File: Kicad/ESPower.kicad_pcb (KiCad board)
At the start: 2 copper layers, 64.9 x 15 mm, 38 parts, among them J1 Input, J2 Power Switch, J3 Output, J4 Battery, J5 GPIO, Q1 DMP2035U-7, Q2 FS8205A, SW1 PowerPath enable, SW2 A, SW3 B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

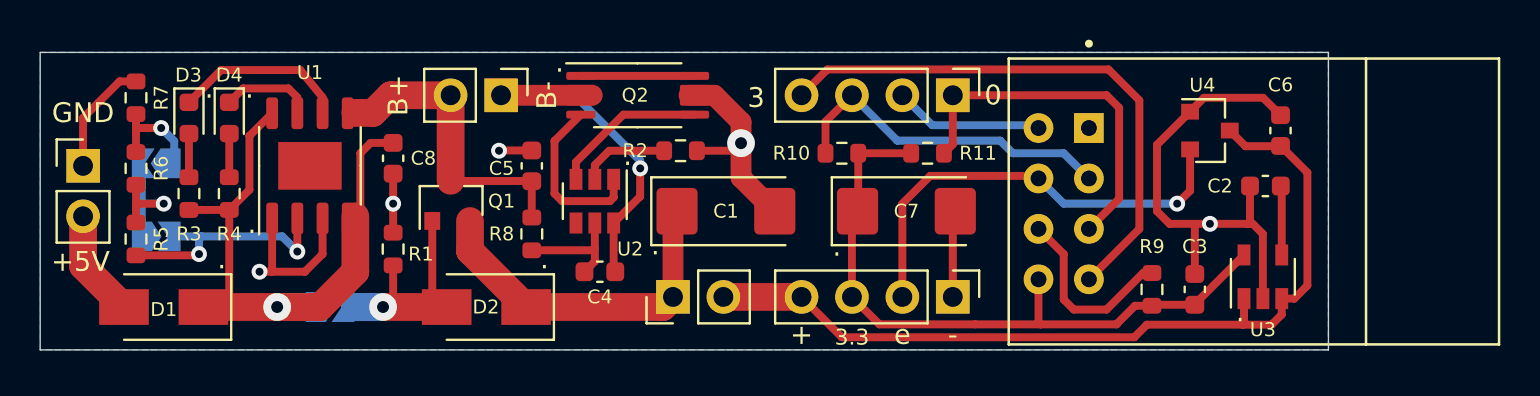
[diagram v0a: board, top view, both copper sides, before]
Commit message: Switched Q2 footprint
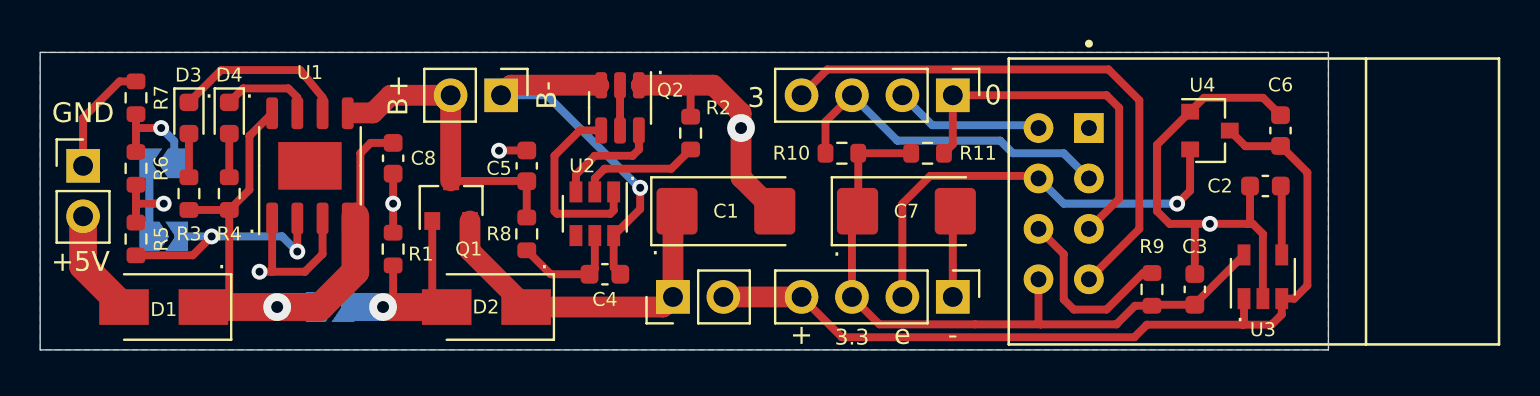
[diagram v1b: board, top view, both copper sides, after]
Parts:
- Q2: footprint Package_SO:TSSOP-8_4.4x3mm_P0.65mm -> Package_TO_SOT_SMD:SOT-23-6
- moved Q2 1.09 mm to (112.4, 96.8), turned to -90 degrees
- moved R2 1.02 mm to (116.0, 98.0), turned to 90 degrees
- moved U2 0.64 mm to (111.1, 102.1)
- moved SW2 0.38 mm to (89.4, 103.3)
- moved SW3 0.38 mm to (89.4, 99.6)
- moved C4 0.28 mm to (111.6, 105.2)
- moved C5 0.25 mm to (107.7, 99.7)
- moved R8 0.25 mm to (107.7, 103.1)
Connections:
- Q2 pad 1: Net-(Q2-Pad1) -> GND
- Q2 pad 2: Net-(C4-Pad2) -> Net-(Q2-Pad2)
- Q2 pad 5: Net-(Q2-Pad5) -> Net-(Q2-Pad2)
- Q2 pad 6: GND -> Net-(U2-Pad3)
- U2 pad 3: Net-(Q2-Pad5) -> Net-(U2-Pad3)
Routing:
- net Net-(Q2-Pad5): track 7.83 -> 0.00 mm
- net Net-(Q2-Pad1): track 5.73 -> 0.00 mm
- net Net-(U2-Pad3): track 0.00 -> 5.53 mm
- net Net-(Q2-Pad2): track 0.00 -> 2.28 mm
- net GND: track 58.1 -> 59.9 mm
- net Net-(R2-Pad1): track 4.51 -> 6.11 mm
- net Net-(U2-Pad1): track 8.66 -> 9.71 mm

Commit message: Resized board
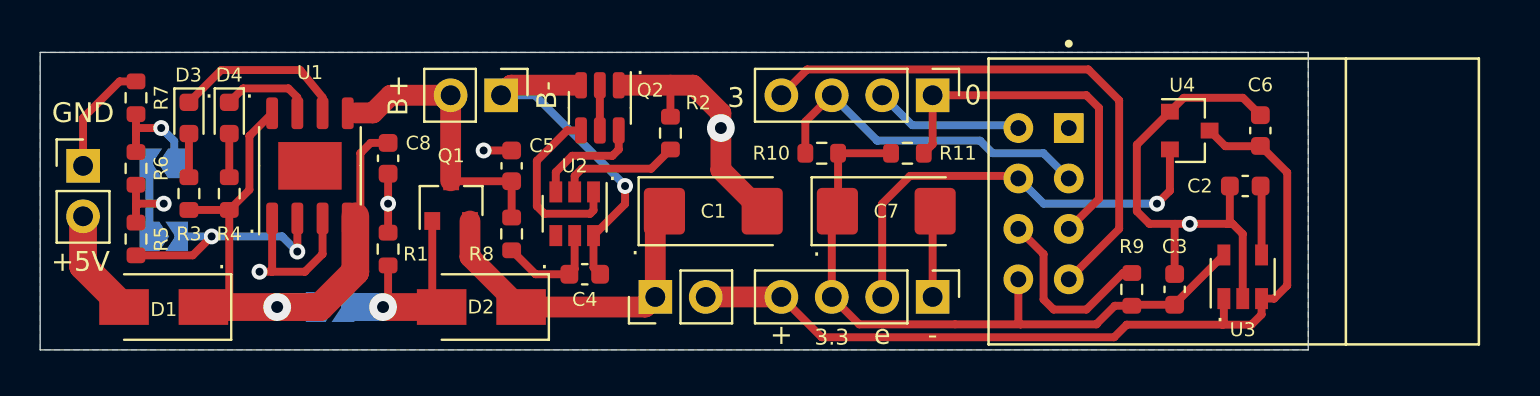
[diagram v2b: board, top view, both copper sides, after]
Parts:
- moved C2 1.02 mm to (143.9, 100.7)
- moved C6 1.02 mm to (144.7, 97.9)
- moved R9 1.02 mm to (138.2, 105.9)
- moved U2 1.02 mm to (110.1, 102.1)
- moved C3 1.02 mm to (140.3, 105.9)
- moved C4 1.02 mm to (110.6, 105.2)
- moved C7 1.02 mm to (125.8, 102.0)
- moved J3 1.02 mm to (128.1, 106.3)
- moved J5 1.02 mm to (128.1, 96.1)
- moved Q2 1.02 mm to (111.4, 96.8)
- moved R10 1.02 mm to (122.6, 99.1)
- moved R11 1.02 mm to (126.9, 99.1)
- moved R2 1.02 mm to (114.9, 98.0)
- moved U3 1.02 mm to (143.8, 105.3)
- moved U4 1.02 mm to (141.1, 97.9)
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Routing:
- net Net-(C4-Pad2): track 19.1 -> 17.3 mm
- net +BATT: track 15.4 -> 14.4 mm
- net Net-(C1-Pad1): track 17.5 -> 16.9 mm
- net Net-(U2-Pad1): track 9.71 -> 9.16 mm
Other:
- board size 64.9 x 15 mm -> 63.9 x 15 mm
